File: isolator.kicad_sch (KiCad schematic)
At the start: 50 parts, among them J1 USB_C_Receptacle_USB2.0_16P, J2 USB_C_Receptacle_PowerOnly_6P, Q1 2N7002, T1 750313638, U1 ADuM4165, U13 TLV7041DBV, U14 TLV7041DBV, U2 NUP4202, U3 NUP4202, U5 SN6505BDBV, U6 MIC29302WU, U7 TPS2121, Y1 24M

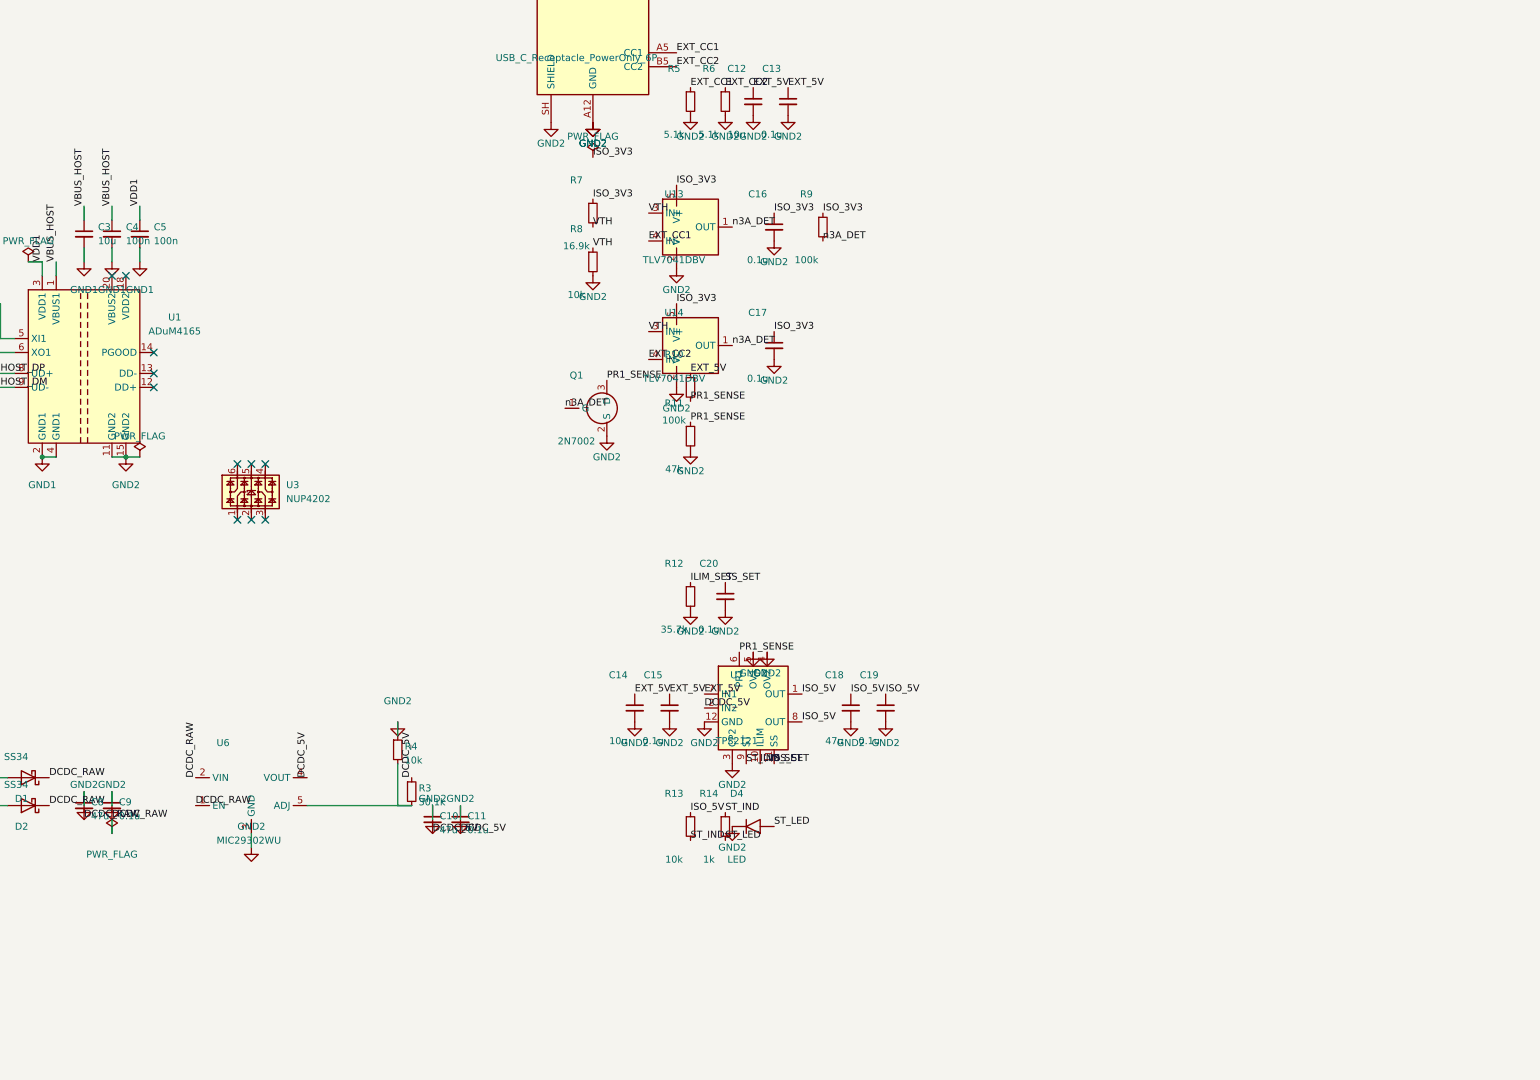
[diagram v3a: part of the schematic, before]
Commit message: feat(sch): ADuM side 2, USB2514B hub core, 3.3V rail
Co-Authored-By: Claude Fable 5 <noreply@anthropic.com>
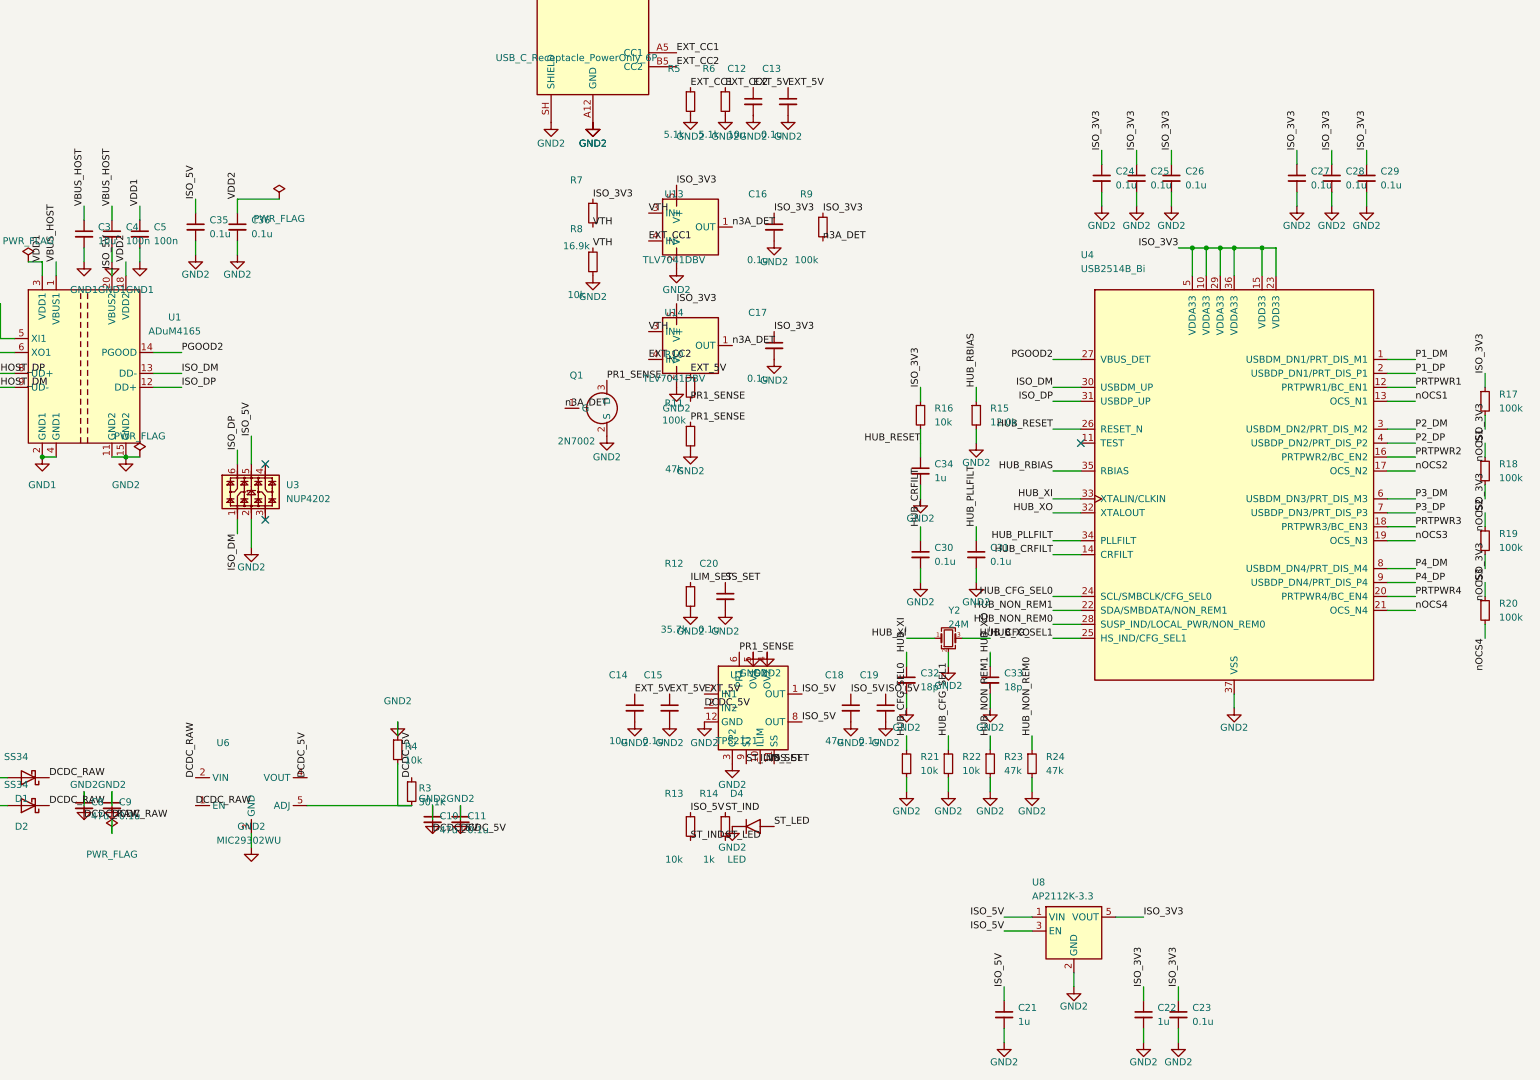
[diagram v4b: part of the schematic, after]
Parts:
- added C21, C22, C34: 1u, symbol Device:C_Small
- added C23, C24, C25, C26, C27, C28, C29, C30, C31, C35, C36: 0.1u, symbol Device:C_Small
- added C32, C33: 18p, symbol Device:C_Small
- added R15: 12.0k, symbol Device:R_Small
- added R16, R21, R22: 10k, symbol Device:R_Small
- added R17, R18, R19, R20: 100k, symbol Device:R_Small
- added R23, R24: 47k, symbol Device:R_Small
- added U4: USB2514B_Bi, symbol Interface_USB:USB2514B_Bi
- added U8: AP2112K-3.3, symbol Regulator_Linear:AP2112K-3.3
- added Y2: 24M, symbol Device:Crystal_GND24_Small
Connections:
- net GND2: now also U3.2, C21.2, C22.2, C23.2, C24.2, C25.2, C26.2, C27.2, C28.2, C29.2, C30.2, C31.2, C32.2, C33.2, C34.2, C35.2, C36.2, R15.2, R21.2, R22.2, R23.2, R24.2, U4.37 (VSS), U8.2 (GND), Y2.2 (G), Y2.4 (G)
- net ISO_3V3: now also C22.1, C23.1, C24.1, C25.1, C26.1, C27.1, C28.1, C29.1, R16.1, R17.1, R18.1, R19.1, R20.1, U4.10 (VDDA33), U4.15 (VDD33), U4.23 (VDD33), U4.29 (VDDA33), U4.36 (VDDA33), U4.5 (VDDA33), U8.5 (VOUT)
- net ISO_5V: now also U1.20 (VBUS2), U3.5, C21.1, C35.1, U8.1 (VIN), U8.3 (EN)
- net ISO_DM: now reaches U3.1
- net ISO_DM: now also U1.13 (DD-), U4.30 (USBDM_UP)
- net ISO_DP: now reaches U3.6
- net ISO_DP: now also U1.12 (DD+), U4.31 (USBDP_UP)
- net PGOOD2: now reaches U1.14 (PGOOD)
- net PGOOD2: now also U4.27 (VBUS_DET)
- net VDD2: now reaches U1.18 (VDD2)
- net VDD2: now also C36.1
- new net HUB_CFG_SEL0: R21.1, U4.24 (SCL/SMBCLK/CFG_SEL0)
- new net HUB_CFG_SEL1: R22.1, U4.25 (HS_IND/CFG_SEL1)
- new net HUB_CRFILT: C30.1, U4.14 (CRFILT)
- new net HUB_NON_REM0: R24.1, U4.28 (SUSP_IND/LOCAL_PWR/NON_REM0)
- new net HUB_NON_REM1: R23.1, U4.22 (SDA/SMBDATA/NON_REM1)
- new net HUB_PLLFILT: C31.1, U4.34 (PLLFILT)
- new net HUB_RBIAS: R15.1, U4.35 (RBIAS)
- new net HUB_RESET: C34.1, R16.2, U4.26 (RESET_N)
- new net HUB_XI: C32.1, U4.33 (XTALIN/CLKIN), Y2.1
- new net HUB_XO: C33.1, U4.32 (XTALOUT), Y2.3
- new net P1_DM: U4.1 (USBDM_DN1/PRT_DIS_M1)
- new net P1_DP: U4.2 (USBDP_DN1/PRT_DIS_P1)
- new net P2_DM: U4.3 (USBDM_DN2/PRT_DIS_M2)
- new net P2_DP: U4.4 (USBDP_DN2/PRT_DIS_P2)
- new net P3_DM: U4.6 (USBDM_DN3/PRT_DIS_M3)
- new net P3_DP: U4.7 (USBDP_DN3/PRT_DIS_P3)
- new net P4_DM: U4.8 (USBDM_DN4/PRT_DIS_M4)
- new net P4_DP: U4.9 (USBDP_DN4/PRT_DIS_P4)
- new net PRTPWR1: U4.12 (PRTPWR1/BC_EN1)
- new net PRTPWR2: U4.16 (PRTPWR2/BC_EN2)
- new net PRTPWR3: U4.18 (PRTPWR3/BC_EN3)
- new net PRTPWR4: U4.20 (PRTPWR4/BC_EN4)
- new net nOCS1: R17.2, U4.13 (OCS_N1)
- new net nOCS2: R18.2, U4.17 (OCS_N2)
- new net nOCS3: R19.2, U4.19 (OCS_N3)
- new net nOCS4: R20.2, U4.21 (OCS_N4)
- no-connect marks 15 -> 7

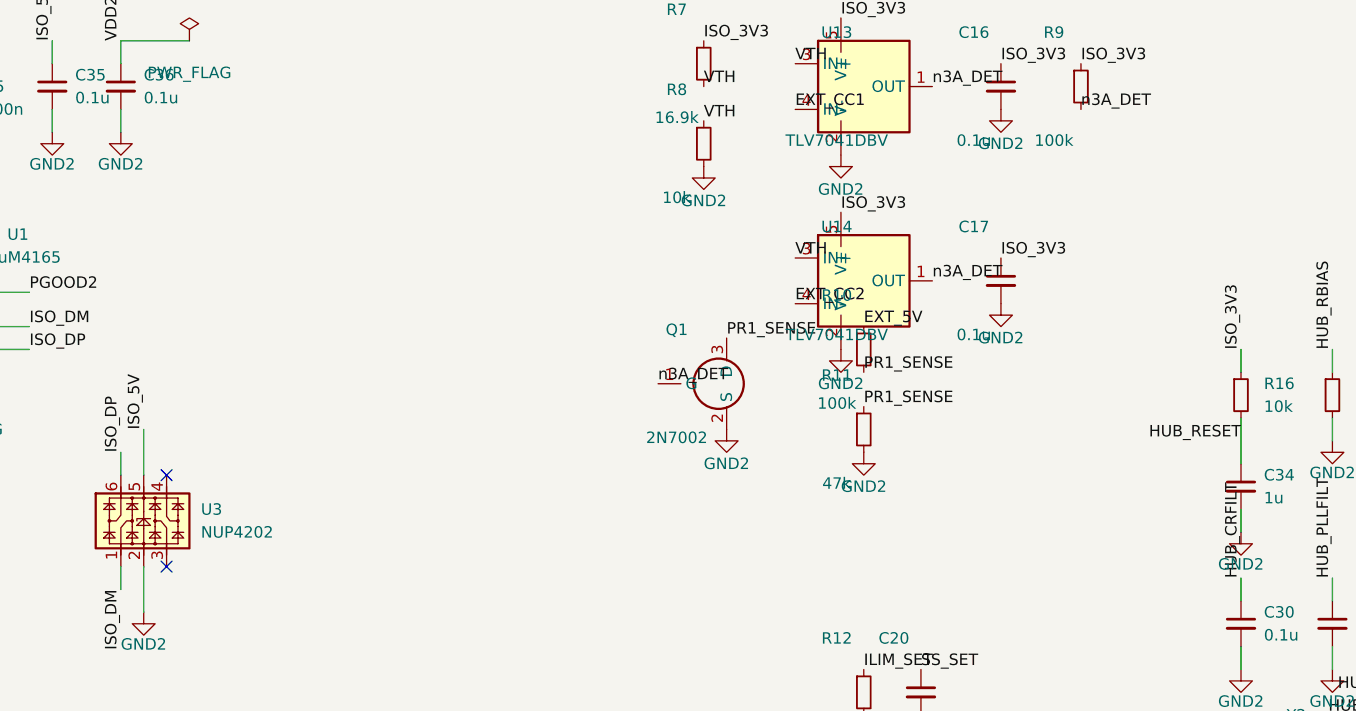
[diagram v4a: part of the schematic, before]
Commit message: fix(sch): PGOOD2 provisions, reset discharge diode, self-powered doc
Co-Authored-By: Claude Fable 5 <noreply@anthropic.com>
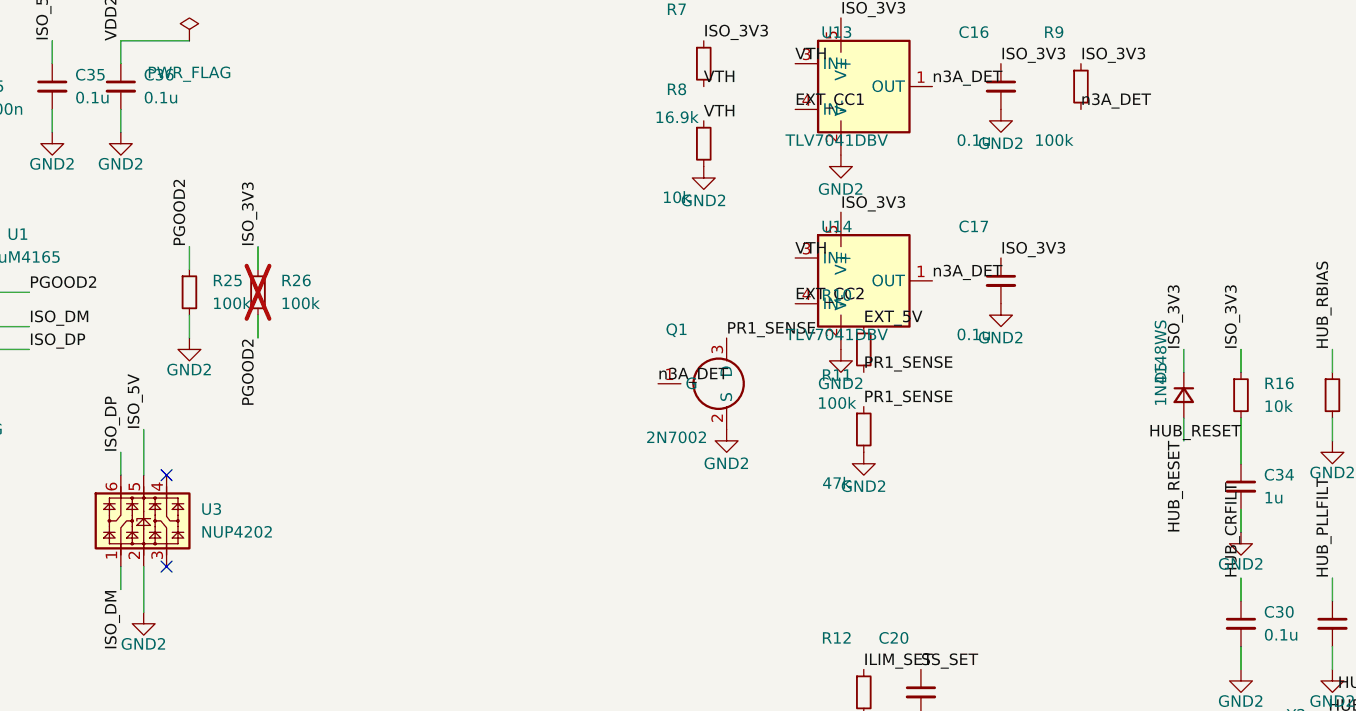
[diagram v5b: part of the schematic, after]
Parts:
- added D5: 1N4148WS, symbol Device:D_Small
- added R25, R26: 100k, symbol Device:R_Small
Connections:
- net GND2: now also R25.2
- net HUB_RESET: now also D5.2 (A)
- net ISO_3V3: now also D5.1 (K), R26.1
- net PGOOD2: now also R25.1, R26.2

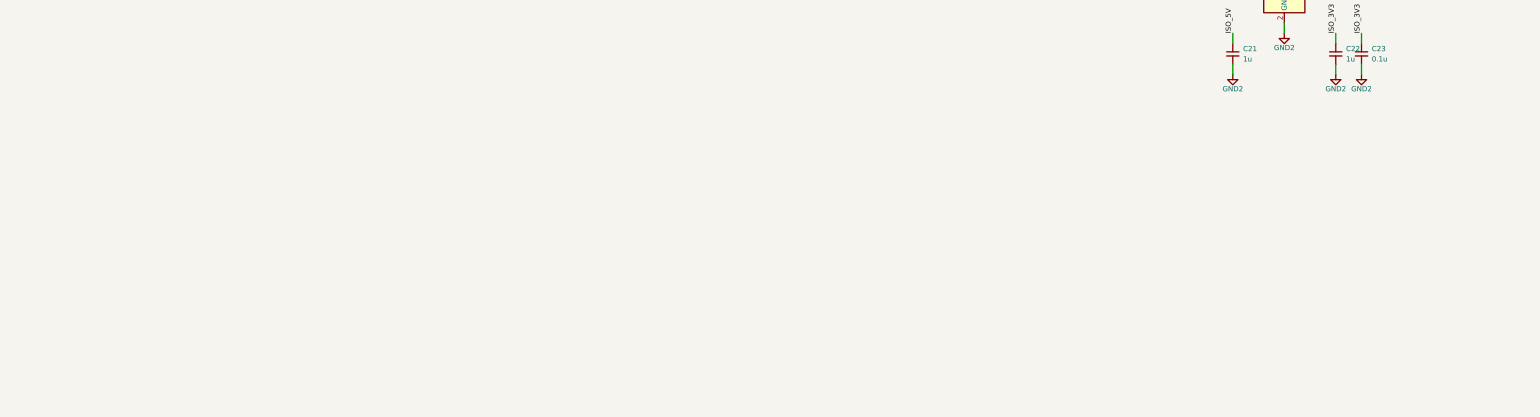
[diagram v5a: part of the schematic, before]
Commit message: feat(sch): 4 downstream ports with per-port current limiting
Add U9-U12 (TPS2553DBV power switches, R_ILIM=40.2k -> ~649mA nominal
current limit per datasheet eq.), U15-U18 (NUP4202 ESD), J3/J4 (USB-A),
J5/J6 (USB-C with CC1/CC2 56k pull-ups to own VBUS), and per-port VBUS
bulk decoupling. Wired to the Task 7 hub label stubs by matching label
text. ERC: 0 errors; the 12 isolated_pin_label warnings from Task 7 are
gone.

Co-Authored-By: Claude Fable 5 <noreply@anthropic.com>
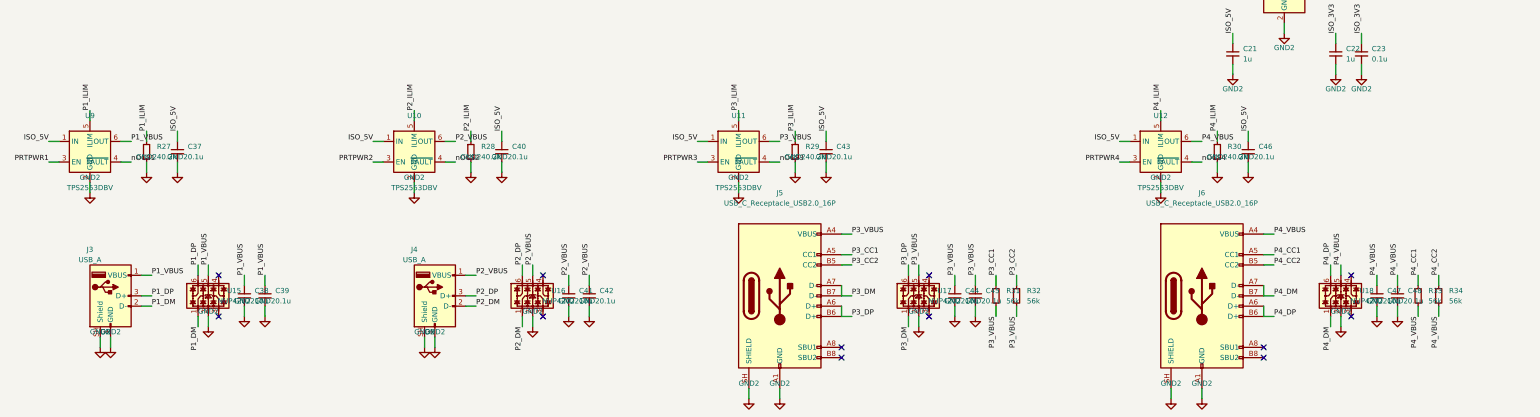
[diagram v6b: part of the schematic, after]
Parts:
- added C37, C39, C40, C42, C43, C45, C46, C48: 0.1u, symbol Device:C_Small
- added C38, C41, C44, C47: 10u, symbol Device:C_Small
- added J3, J4: USB_A, symbol Connector:USB_A
- added J5, J6: USB_C_Receptacle_USB2.0_16P, symbol Connector:USB_C_Receptacle_USB2.0_16P
- added R27, R28, R29, R30: 40.2k, symbol Device:R_Small
- added R31, R32, R33, R34: 56k, symbol Device:R_Small
- added U10, U11, U12, U9: TPS2553DBV, symbol isolator-lib:TPS2553DBV
- added U15, U16, U17, U18: NUP4202, Package_TO_SOT_SMD:SOT-363_SC-70-6, symbol Power_Protection:NUP4202
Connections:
- net GND2: now also C37.2, C38.2, C39.2, C40.2, C41.2, C42.2, C43.2, C44.2, C45.2, C46.2, C47.2, C48.2, J3.4 (GND), J3.SH (Shield), J4.4 (GND), J4.SH (Shield), J5.A1 (GND), J5.A12 (GND), J5.B1 (GND), J5.B12 (GND), J5.SH (SHIELD), J6.A1 (GND), J6.A12 (GND), J6.B1 (GND), J6.B12 (GND), J6.SH (SHIELD), R27.2, R28.2, R29.2, R30.2, U10.2 (GND), U11.2 (GND), U12.2 (GND), U15.2, U16.2, U17.2, U18.2, U9.2 (GND)
- net ISO_5V: now also C37.1, C40.1, C43.1, C46.1, U10.1 (IN), U11.1 (IN), U12.1 (IN), U9.1 (IN)
- net P1_DM: now also J3.2 (D-), U15.1
- net P1_DP: now also J3.3 (D+), U15.6
- net P2_DM: now also J4.2 (D-), U16.1
- net P2_DP: now also J4.3 (D+), U16.6
- net P3_DM: now also J5.A7 (D-), J5.B7 (D-), U17.1
- net P3_DP: now also J5.A6 (D+), J5.B6 (D+), U17.6
- net P4_DM: now also J6.A7 (D-), J6.B7 (D-), U18.1
- net P4_DP: now also J6.A6 (D+), J6.B6 (D+), U18.6
- net PRTPWR1: now also U9.3 (EN)
- net PRTPWR2: now also U10.3 (EN)
- net PRTPWR3: now also U11.3 (EN)
- net PRTPWR4: now also U12.3 (EN)
- net nOCS1: now also U9.4 (~{FAULT})
- net nOCS2: now also U10.4 (~{FAULT})
- net nOCS3: now also U11.4 (~{FAULT})
- net nOCS4: now also U12.4 (~{FAULT})
- new net P1_ILIM: R27.1, U9.5 (ILIM)
- new net P1_VBUS: C38.1, C39.1, J3.1 (VBUS), U15.5, U9.6 (OUT)
- new net P2_ILIM: R28.1, U10.5 (ILIM)
- new net P2_VBUS: C41.1, C42.1, J4.1 (VBUS), U10.6 (OUT), U16.5
- new net P3_CC1: J5.A5 (CC1), R31.1
- new net P3_CC2: J5.B5 (CC2), R32.1
- new net P3_ILIM: R29.1, U11.5 (ILIM)
- new net P3_VBUS: C44.1, C45.1, J5.A4 (VBUS), J5.A9 (VBUS), J5.B4 (VBUS), J5.B9 (VBUS), R31.2, R32.2, U11.6 (OUT), U17.5
- new net P4_CC1: J6.A5 (CC1), R33.1
- new net P4_CC2: J6.B5 (CC2), R34.1
- new net P4_ILIM: R30.1, U12.5 (ILIM)
- new net P4_VBUS: C47.1, C48.1, J6.A4 (VBUS), J6.A9 (VBUS), J6.B4 (VBUS), J6.B9 (VBUS), R33.2, R34.2, U12.6 (OUT), U18.5
- no-connect marks 7 -> 19
